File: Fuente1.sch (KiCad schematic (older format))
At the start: 21 parts, among them J1 Alimentacion, J2 Salidas de voltaje, T1 5:1 / 5A, U1 L7812CV, U2 L7912CV, U3 LM338T, U4 L7805CV

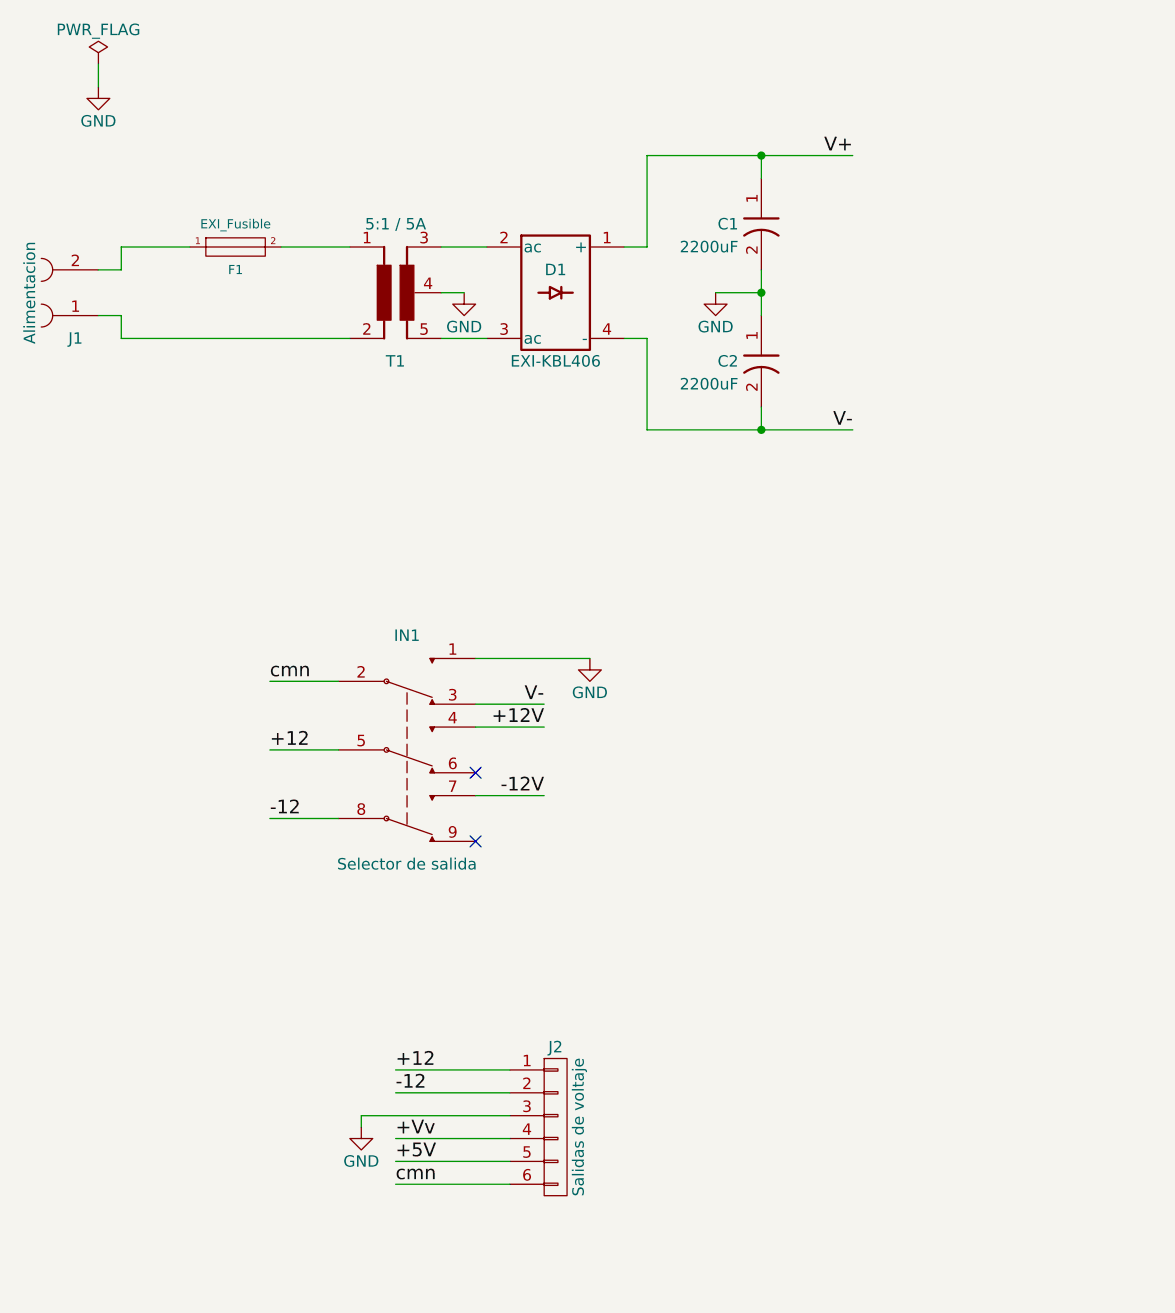
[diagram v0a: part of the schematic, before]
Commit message: *** Corrección de reguladores ***
 Cambios para hacer commit:
	modificado:    Fuente1.bak
	modificado:    Fuente1.kicad_pcb
	modificado:    Fuente1.kicad_pcb-bak
	modificado:    Fuente1.net
	renombrado:    _saved_Fuente1.sch -> Fuente1.sch
	modificado:    vista1.jpg
	modificado:    vista2.jpg
	nuevo archivo: vista3.jpg
	nuevo archivo: vista4.jpg
	nuevo archivo: vista5.jpg
	nuevo archivo: vista6.jpg
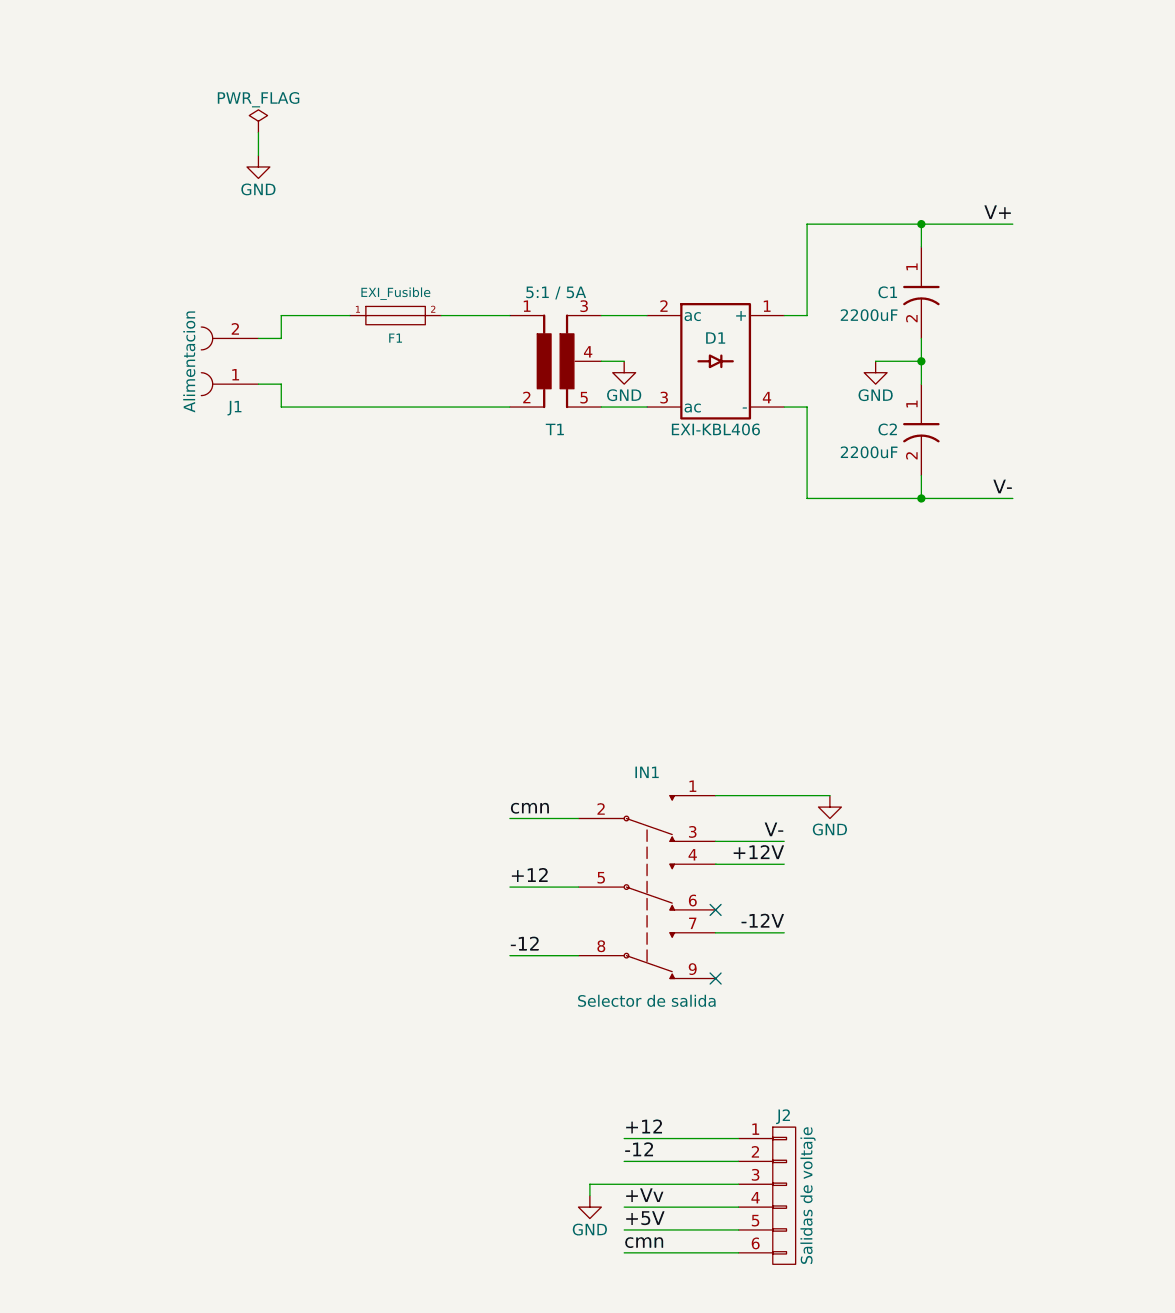
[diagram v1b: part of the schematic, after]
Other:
- moved on the sheet: C1, C2, D1, F1, IN1, J1, J2, T1

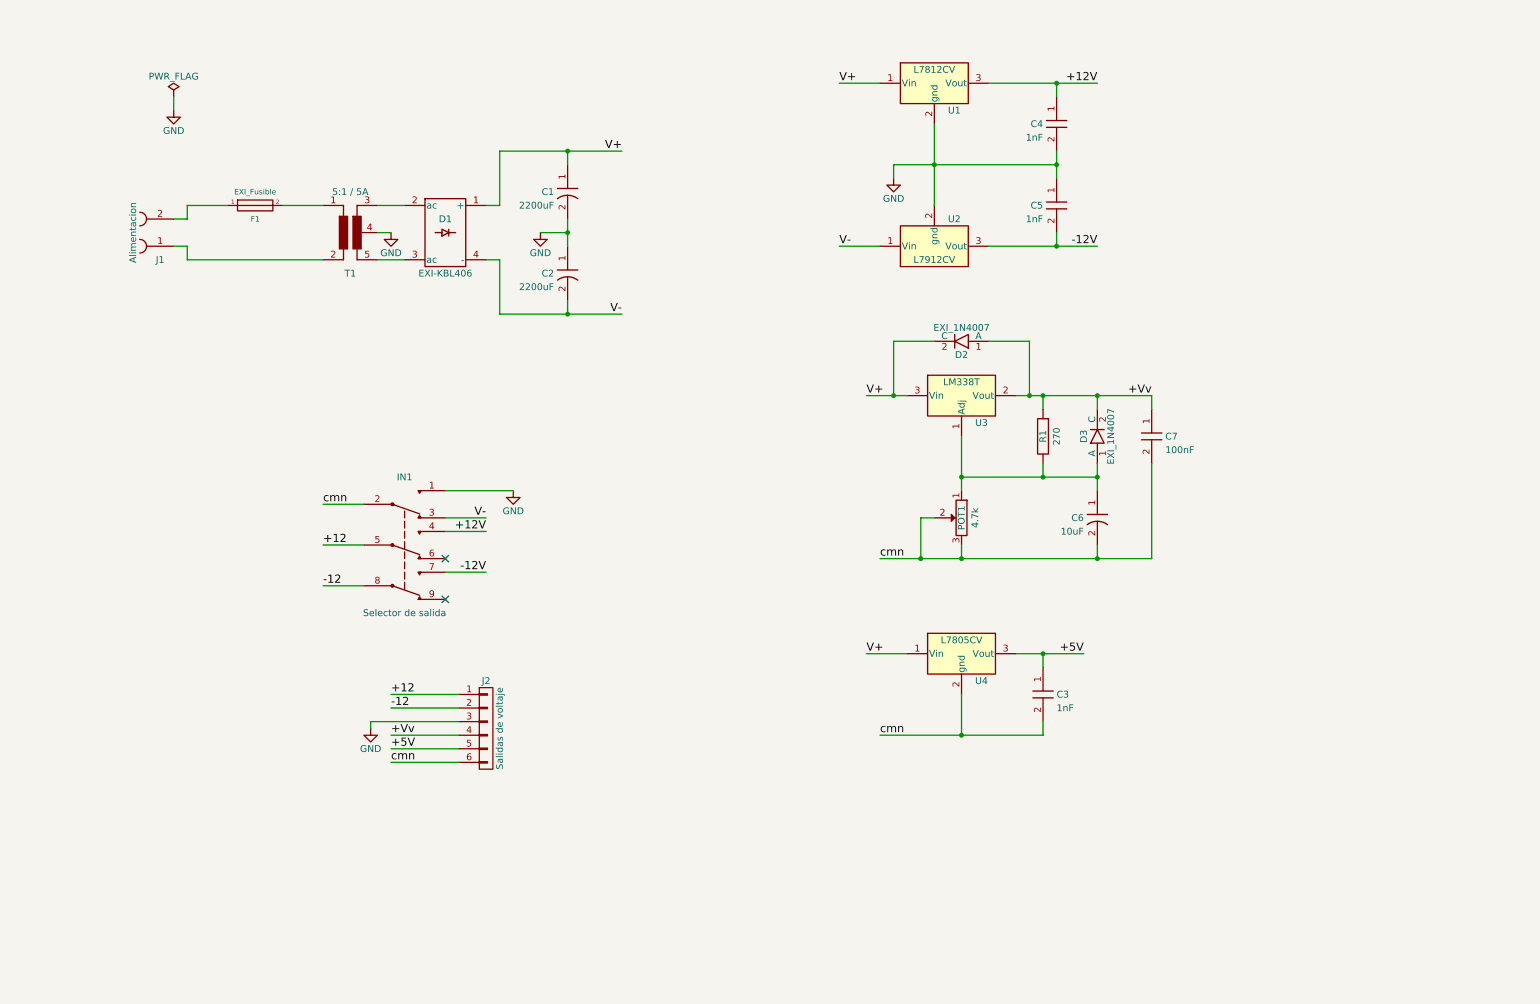
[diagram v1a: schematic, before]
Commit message: Seccionado
Anotaciones de secciones en el esquemático

 Cambios para hacer commit:
	modificado:    Fuente1.bak
	modificado:    Fuente1.sch
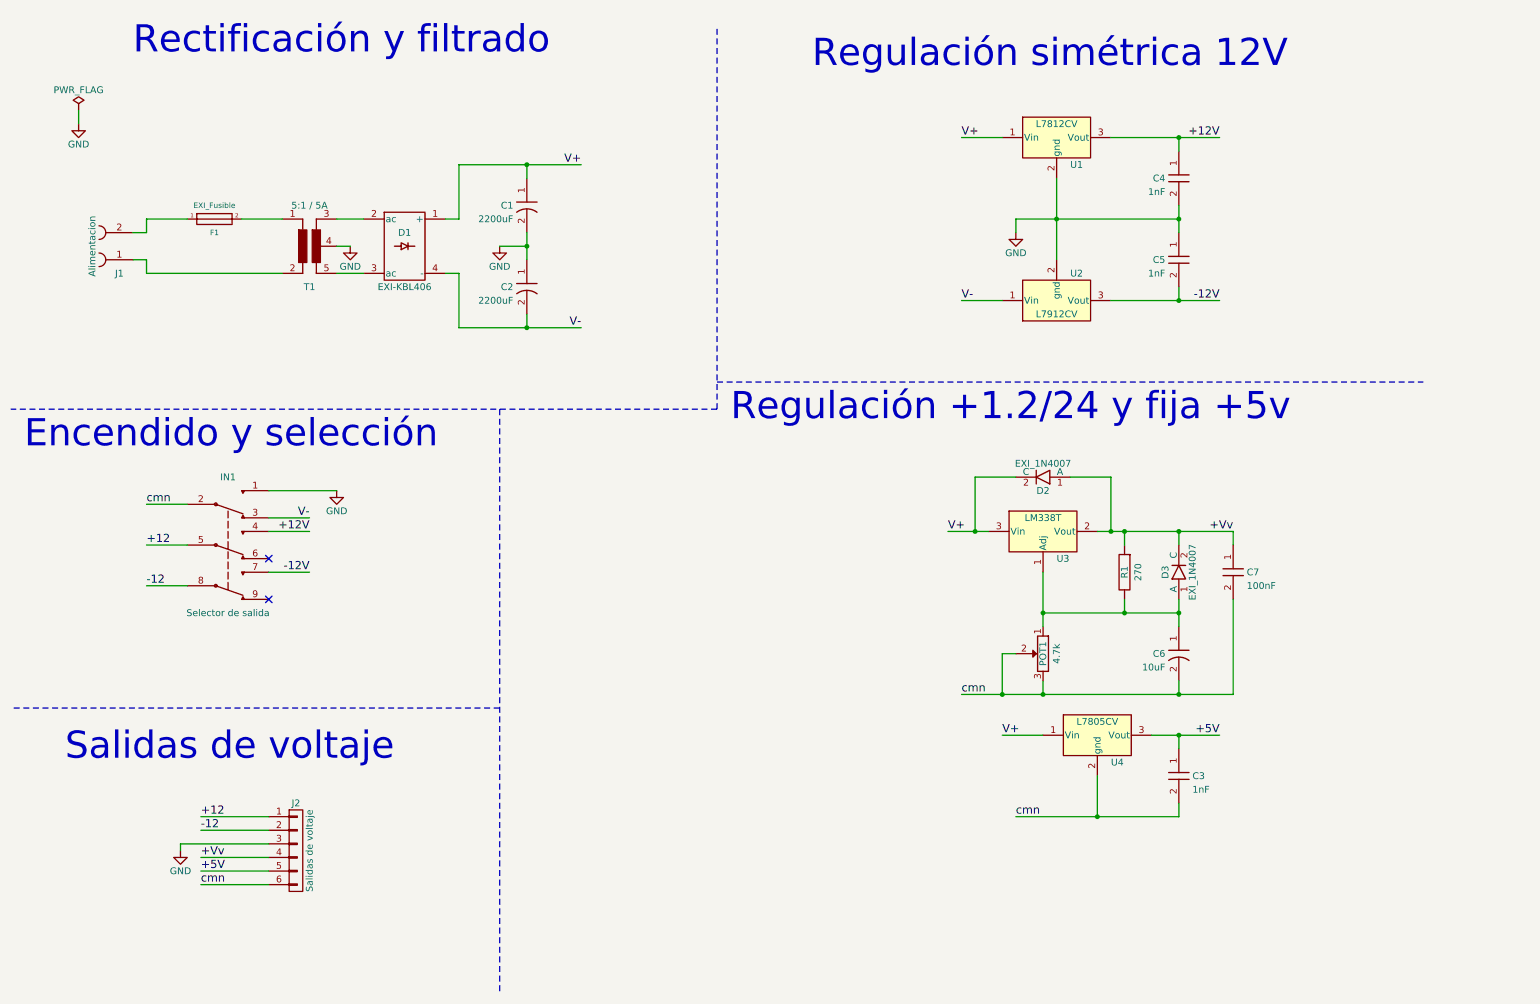
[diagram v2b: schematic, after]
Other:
- note added: "Encendido y selección"
- note added: "Rectificación y filtrado"
- note added: "Regulación +1.2/24 y fija +5v"
- note added: "Regulación simétrica 12V"
- note added: "Salidas de voltaje"
- moved on the sheet: C1, C2, C3, C4, C5, C6, C7, D1, D2, D3, F1, IN1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
